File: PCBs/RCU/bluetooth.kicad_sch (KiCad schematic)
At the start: 31 parts, among them J400 USB_C_Receptacle_USB2.0, Q400 Q_NMOS_DGS, Q401 Q_NMOS_DGS, Q402 Q_PMOS_DGS, Q403 Q_NMOS_DGS, SW400 SW_Push, U400 CH340C, U401 DG2788ADN-T1-GE4, U402 ESP32-MINI-1

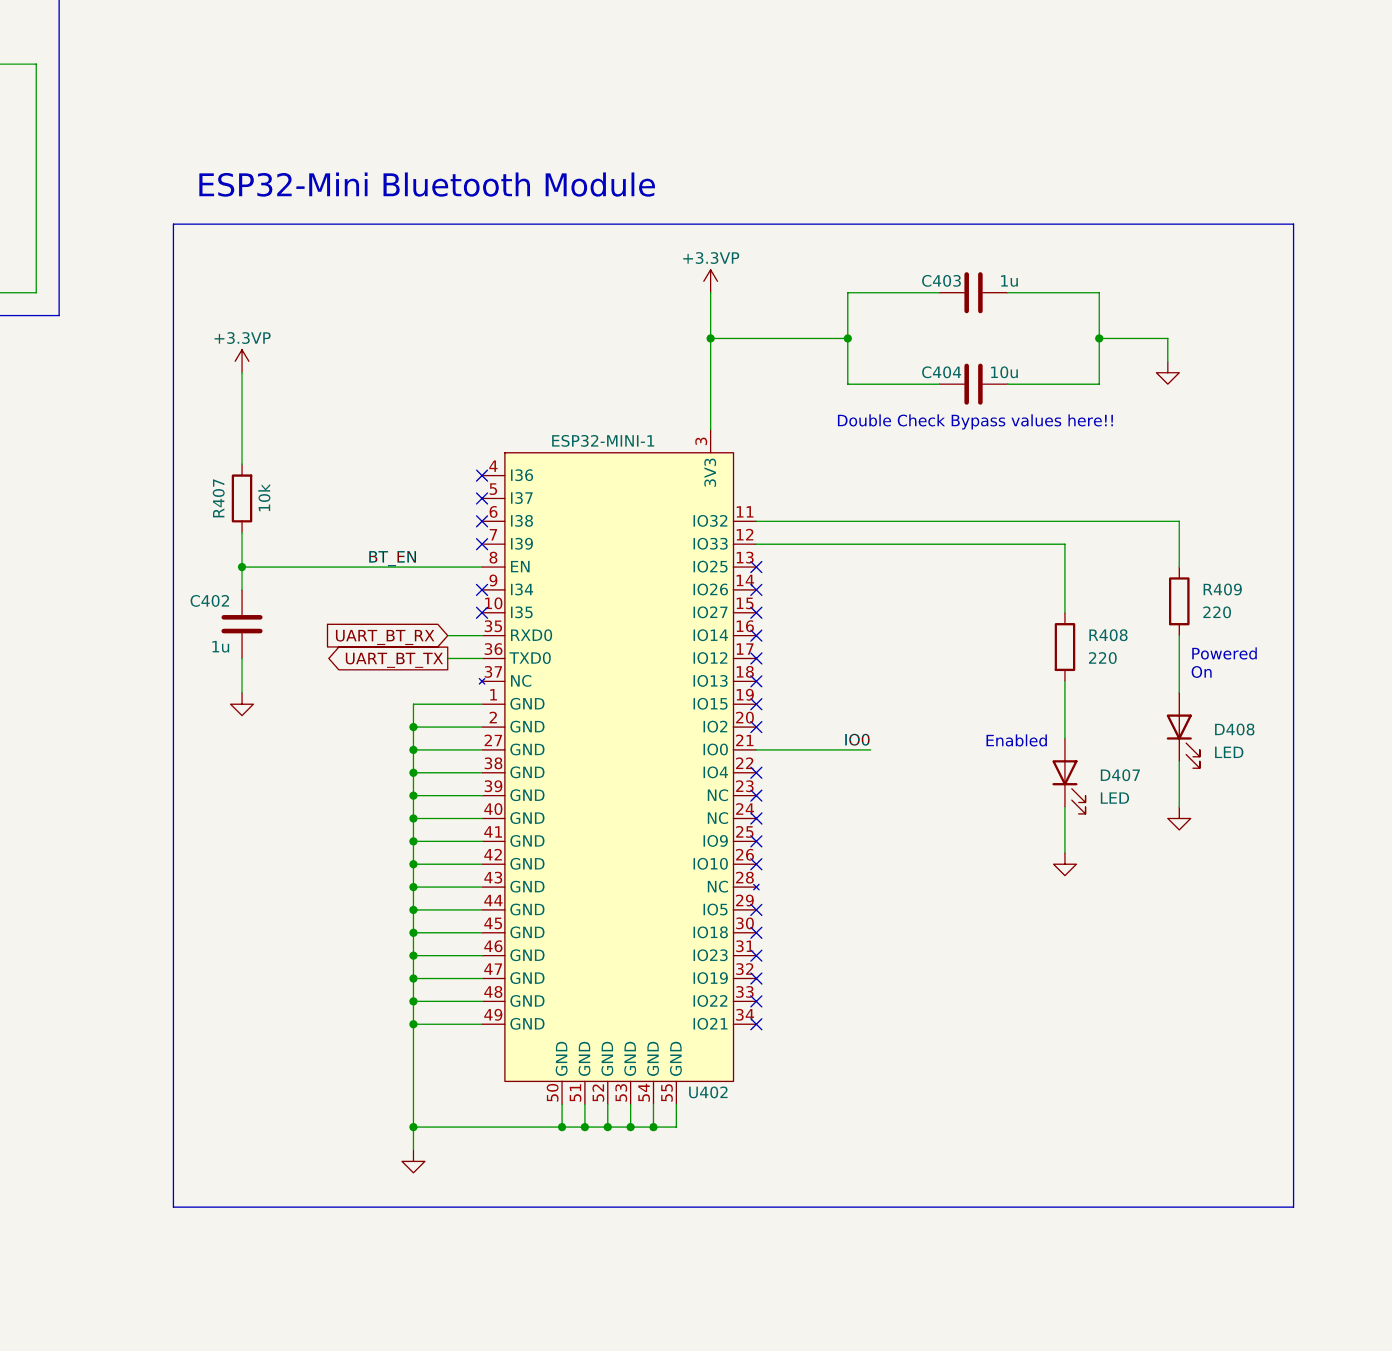
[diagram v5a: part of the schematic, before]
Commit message: Corrected ESP32-Mini bypass caps and added push-button reset circuit
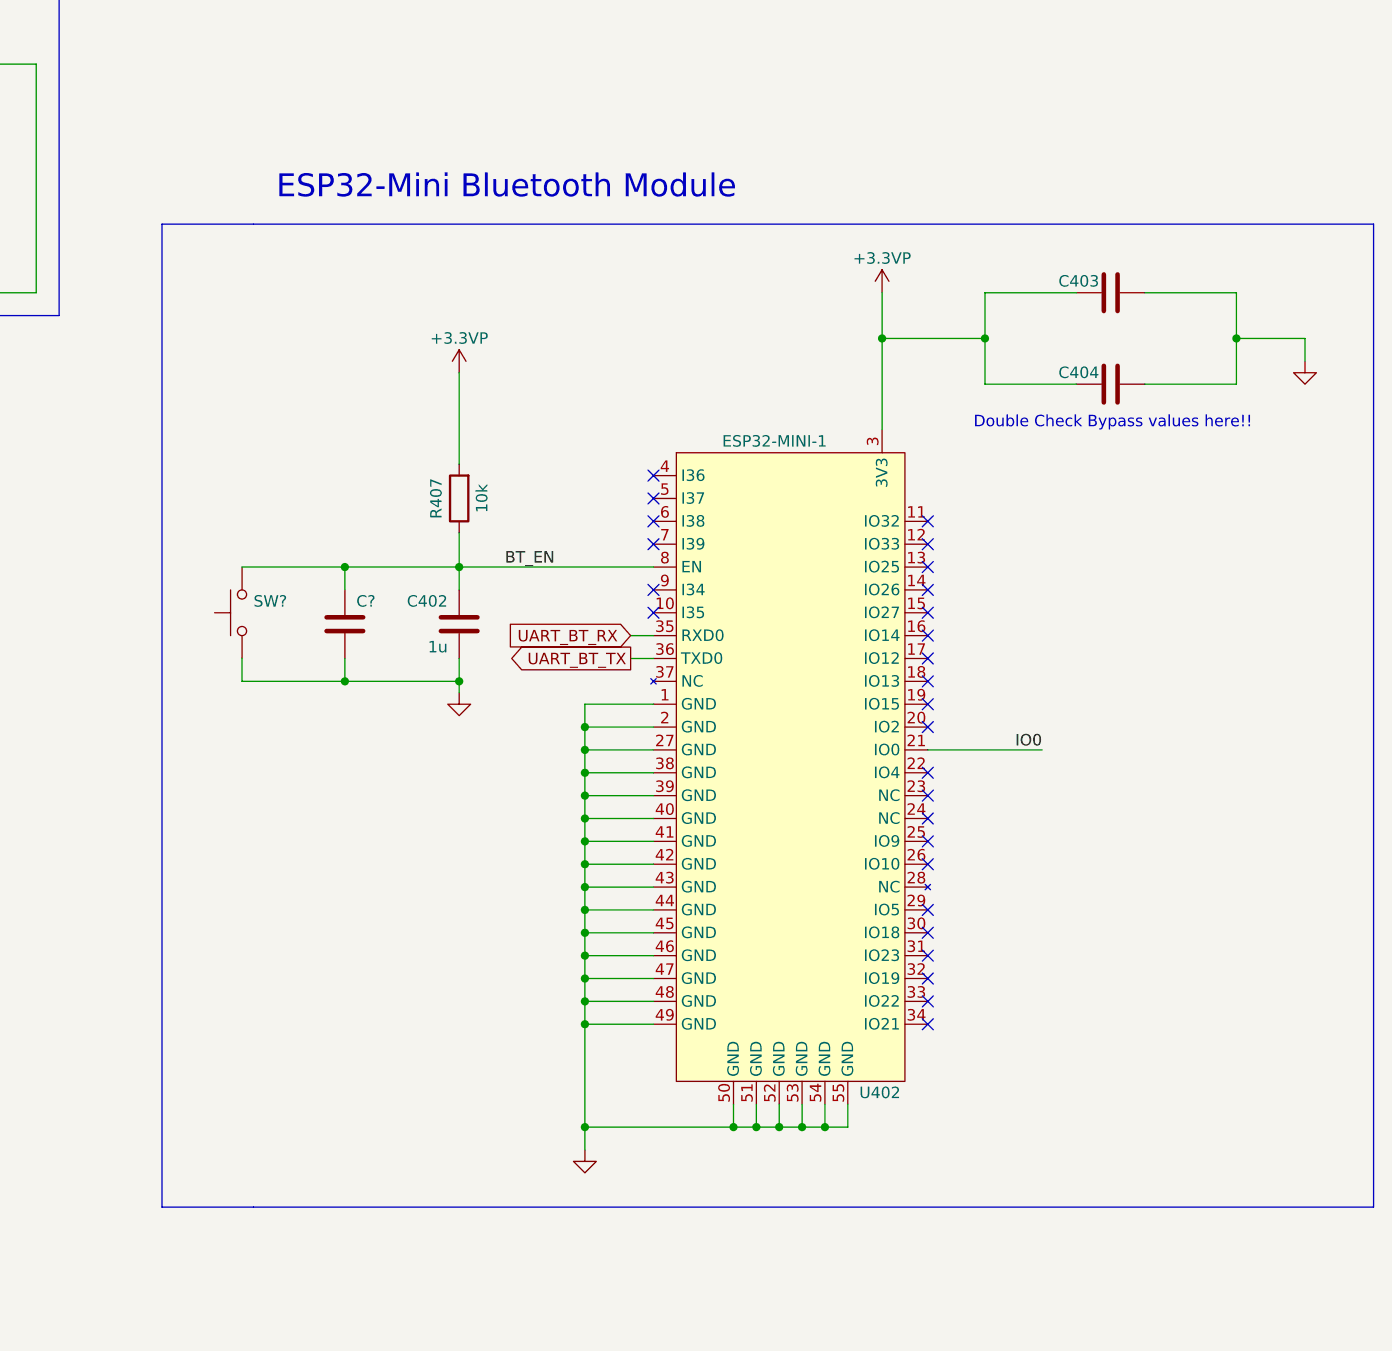
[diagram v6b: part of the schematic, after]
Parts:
- removed D407, D408: LED, symbol Device:LED
- removed R408, R409: 220, symbol Device:R
- added C?: (no value), symbol Device:C
- added SW?: (no value), symbol Switch:SW_Push
- C403: value 1u -> (none)
- C404: value 10u -> (none)
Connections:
- net BT_EN: now also C?.1, SW?.2
- net GND: now also C?.2, SW?.1
- no-connect marks 39 -> 41
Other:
- note removed: "Enabled"
- note removed: "Powered On"
- moved on the sheet: C402, C403, C404, R407, U402

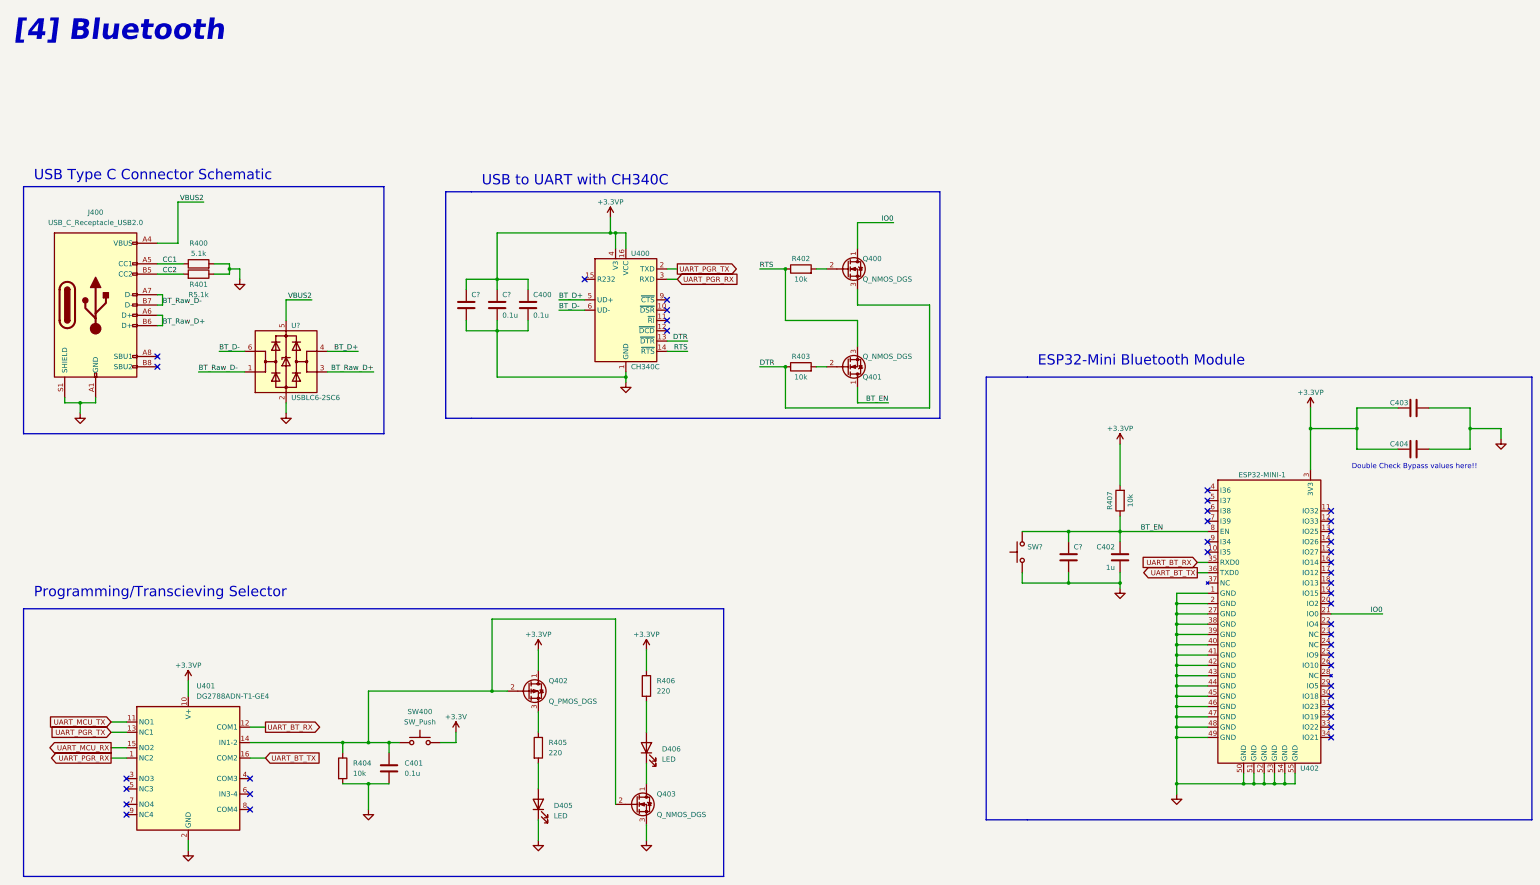
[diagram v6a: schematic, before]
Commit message: Added bypass capacitors to IC switch, the datasheet did not recomend any
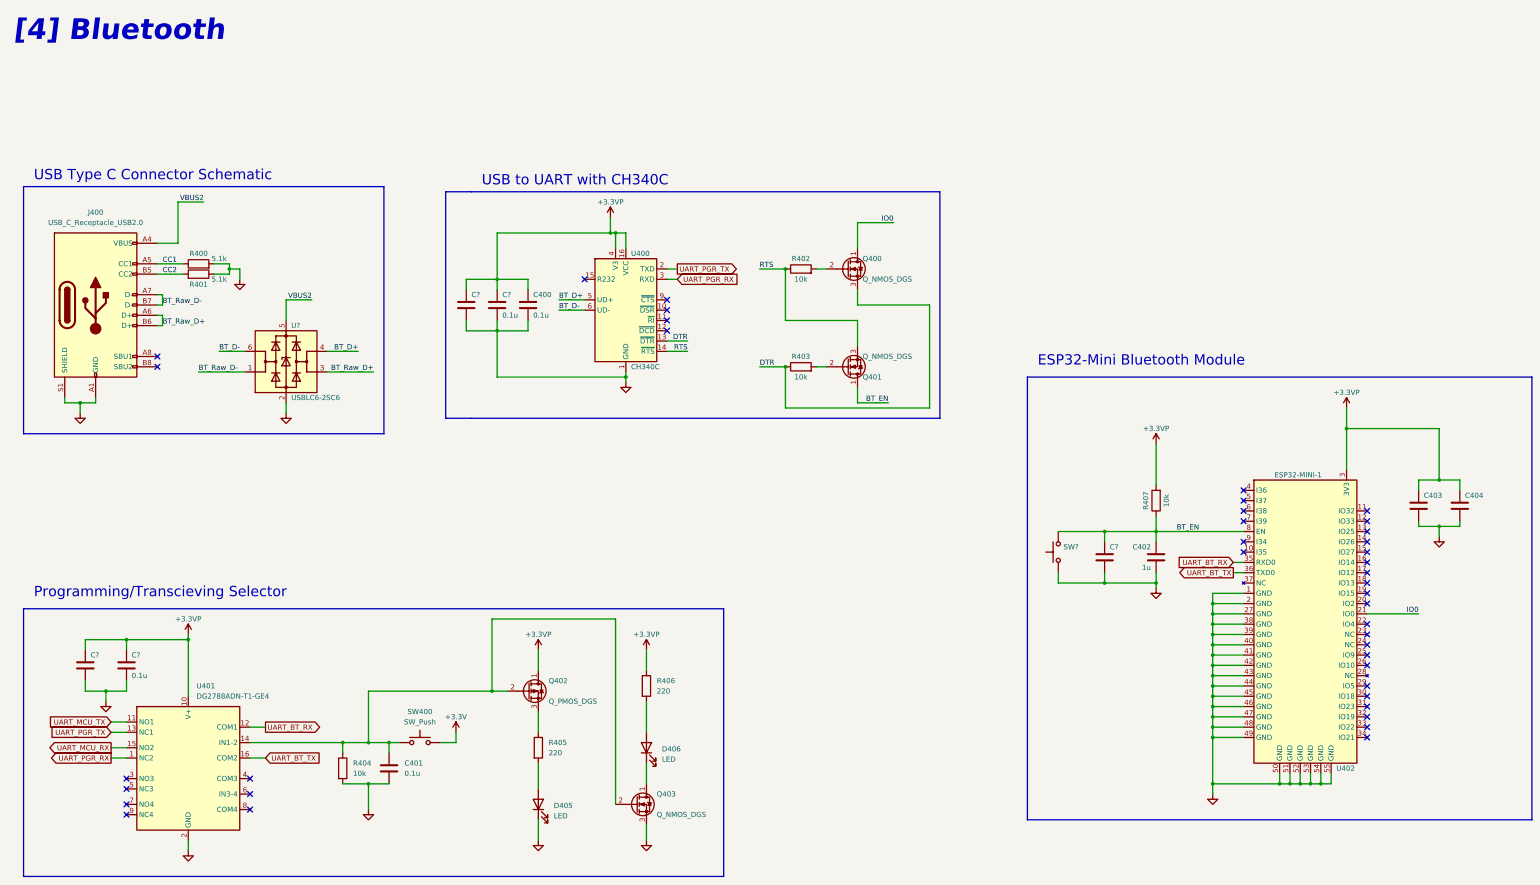
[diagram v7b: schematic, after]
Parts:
- added C?: (no value), symbol Device:C
- added C?: 0.1u, symbol Device:C
- renumbered R5.1k to 5.1k
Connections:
- net +3.3VP: now also C?.1, C?.1
- net GND: now also C?.2, C?.2
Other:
- note removed: "Double Check Bypass values here!!"
- moved on the sheet: C402, C?, R407, SW?, U402

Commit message: Updated ADC schematic to match application note in ADC and op-amp data sheets
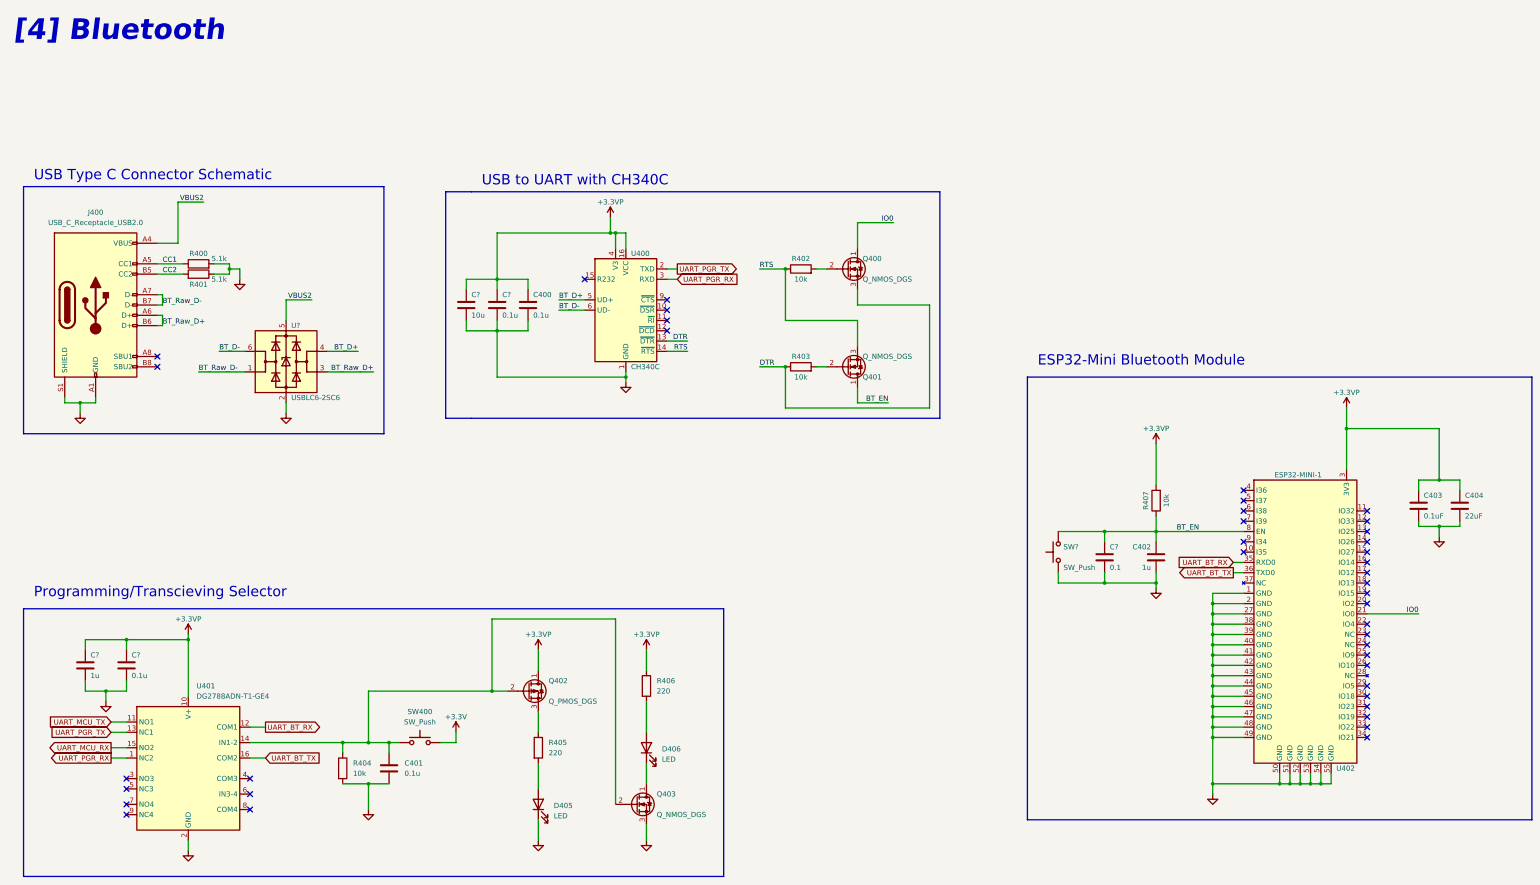
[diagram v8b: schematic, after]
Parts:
- C403: value (none) -> 0.1uF
- C404: value (none) -> 22uF
- C?: value (none) -> 10u
- C?: value (none) -> 1u
- C?: value (none) -> 0.1
- SW?: value (none) -> SW_Push
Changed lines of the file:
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@@
       (effects (font (size 1.27 1.27)) (justify left))
     )
-    (property "Value" "" (id 1) (at 379.73 149.86 0)
+    (property "Value" "0.1uF" (id 1) (at 379.73 149.86 0)
       (effects (font (size 1.27 1.27)) (justify left))
     )
@@
       (effects (font (size 1.27 1.27)) (justify left))
     )
-    (property "Value" "" (id 1) (at 144.78 100.33 0)
+    (property "Value" "10u" (id 1) (at 144.78 100.33 0)
       (effects (font (size 1.27 1.27)) (justify left))
     )
@@
       (effects (font (size 1.27 1.27)) (justify left))
     )
-    (property "Value" "" (id 1) (at 50.8 189.23 0)
+    (property "Value" "1u" (id 1) (at 50.8 189.23 0)
       (effects (font (size 1.27 1.27)) (justify left))
     )
@@
       (effects (font (size 1.27 1.27)) (justify left))
     )
-    (property "Value" "" (id 1) (at 389.89 149.86 0)
+    (property "Value" "22uF" (id 1) (at 389.89 149.86 0)
       (effects (font (size 1.27 1.27)) (justify left))
     )
@@
       (effects (font (size 1.27 1.27)) (justify left))
     )
-    (property "Value" "" (id 1) (at 302.26 162.56 0)
+    (property "Value" "0.1" (id 1) (at 302.26 162.56 0)
       (effects (font (size 1.27 1.27)) (justify left))
     )
@@
       (effects (font (size 1.27 1.27)) (justify right))
     )
-    (property "Value" "" (id 1) (at 290.83 162.56 90)
+    (property "Value" "SW_Push" (id 1) (at 290.83 162.56 90)
       (effects (font (size 1.27 1.27)) (justify right))
     )
